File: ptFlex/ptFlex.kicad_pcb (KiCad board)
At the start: 4 copper layers, 30 x 73.5 mm, 70 parts, among them J1 6 Pin Male Header, J2 8 Pin Male Header, Q1 BSS138, Q2 BSS138, Q3 BSS138, Q4 MMBT3904, Q5 DMP2004K-7, U1 LP3985IM5-3.3/NOPB, U2 ATMega 328p-AU, U3 SA818S-V, U4 ATGM336H-5N31, Y1 8MHz

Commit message: Schematic mostly revised for v2.0
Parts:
- removed ANT2a1, ANT2b1: VHF Test Point, Custom DS:Small Test Point Pin
- removed D2: CDBA340L-G Schottky, Diode_SMD:D_SMA
- removed D3: 5.1V Zenor, Diode_SMD:D_SOD-123
- removed J2: 8 Pin Male Header, Connector_PinHeader_2.54mm:PinHeader_2x04_P2.54mm_Vertical
- removed JPV2, PV1: 5.5V 180mW Solar, Custom DS:PowerFilm MPT3.6-75
- removed R14, R15: 10k, Resistor_SMD:R_0805_2012Metric
- added C21: 2.2uF, Capacitor_SMD:C_0805_2012Metric, F.Cu at (215.6, 70.7)
- added C22: 10nF, Capacitor_SMD:C_0805_2012Metric, F.Cu at (215.6, 73.7)
- added C23: 10nF, Capacitor_SMD:C_0805_2012Metric, F.Cu at (215.6, 76.7)
- added C24: 10nF, Capacitor_SMD:C_0805_2012Metric, F.Cu at (215.6, 79.8)
- added J4: Qwiic, Connector_JST:JST_SH_SM04B-SRSS-TB_1x04-1MP_P1.00mm_Horizontal, F.Cu at (108.9, 133.5)
- added J5: 3 Pin Male Header, Connector_PinHeader_2.54mm:PinHeader_1x03_P2.54mm_Vertical, F.Cu at (82.0, 106.4)
- added J6: Barrel_Jack_Switch, Connector_BarrelJack:BarrelJack_CLIFF_FC681465S_SMT_Horizontal, F.Cu at (106.7, 69.4)
- added PZ1: Piezo Buzzer, Buzzer_Beeper:Buzzer_TDK_PS1240P02BT_D12.2mm_H6.5mm, F.Cu at (103.2, 149.5)
- added SW1: Reset Switch, Button_Switch_SMD:SW_SPST_PTS647_Sx38, F.Cu at (93.8, 142.5)
- added U5: LM1086-5.0, Package_TO_SOT_SMD:TO-263-3_TabPin2, F.Cu at (106.8, 87.5)
- added U6: BME280, Package_LGA:Bosch_LGA-8_2.5x2.5mm_P0.65mm_ClockwisePinNumbering, F.Cu at (215.6, 83.5)
- C1: value 6V 1F -> 10nF; footprint Custom DS:CDS CSP Super Cap 8mm dia -> Capacitor_SMD:C_0805_2012Metric; moved to F.Cu
- D1: value CDBA340L-G Schottky -> 1N4007FL; footprint Diode_SMD:D_SMA -> Diode_SMD:D_SOD-123
- Q3: value BSS138 -> MMBT3904
- R1: value 47 -> 1k; footprint Resistor_SMD:R_2512_6332Metric -> Resistor_SMD:R_0805_2012Metric
- U3: moved to F.Cu
- Y1: value 8MHz -> 16MHz
- moved U3 88.9 mm to (65.7, 94.9), turned to 180 degrees
- moved ANT2 88.9 mm to (56.6, 63.5)
- moved U4 85.8 mm to (61.6, 142.1)
- moved Q3 85.6 mm to (227.2, 63.9)
- moved ANT1 84.5 mm to (64.2, 155.3)
- moved D1 83.3 mm to (221.8, 63.1), turned to 0 degrees
- moved C19 82.8 mm to (65.1, 66.3), turned to -90 degrees
- moved C18 80.2 mm to (68.1, 66.3), turned to -90 degrees
- moved C20 80.1 mm to (60.9, 131.9)
- moved Q5 80.1 mm to (65.2, 131.9)
- moved R23 80.1 mm to (69.4, 131.9)
- moved L3 78.1 mm to (66.1, 69.8), turned to -135 degrees
- moved R10 77.8 mm to (75.1, 145.2)
- moved R11 77.8 mm to (75.1, 143.2)
- moved Q1 77.8 mm to (80.1, 144.2)
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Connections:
- C1 pad 1: Net-(D1-K) -> Net-(D4-K)
- C12 pad 1: +3.3V -> Net-(Q5-D)
- C2 pad 1: /BATT-SENSE -> Net-(C2-Pad1)
- C3 pad 1: +BATT -> +5V
- C4 pad 1: +BATT -> +5V
- C5 pad 1: +BATT -> +5V
- C6 pad 1: +BATT -> +5V
- D1 pad 1: Net-(D1-K) -> +5V
- D4 pad 1: +BATT -> Net-(D4-K)
- D4 pad 2: Net-(D1-K) -> Net-(D4-A)
- J1 pad 2: +BATT -> +5V
- Q3 pad 1: +3.3V -> Net-(Q3-B)
- Q3 pad 2: Net-(Q3-S) -> GND
- Q3 pad 3: Net-(Q3-D) -> Net-(D1-A)
- R1 pad 1: Net-(D1-K) -> Net-(Q3-B)
- R1 pad 2: +BATT -> /PIEZO
- R11 pad 2: +BATT -> +5V
- R13 pad 2: +BATT -> +5V
- R18 pad 2: +BATT -> +5V
- R2 pad 1: /BATT-SENSE -> Net-(C2-Pad1)
- R2 pad 2: +BATT -> Net-(D4-K)
- R22 pad 2: Net-(Q1-D) -> Net-(U2-PD4)
- R3 pad 2: /BATT-SENSE -> Net-(C2-Pad1)
- R7 pad 1: +3.3V -> +5V
- R8 pad 2: /SCL -> Net-(J4-Pin_4)
- R9 pad 2: /SDA -> Net-(J4-Pin_3)
- U1 pad 1: +BATT -> +5V
- U1 pad 3: +BATT -> +5V
- U2 pad 13: Net-(Q2-S) -> Net-(U2-PB1)
- U2 pad 14: Net-(Q3-S) -> Net-(U2-PB2)
- U2 pad 18: +3.3V -> +5V
- U2 pad 2: Net-(Q1-S) -> Net-(U2-PD4)
- U2 pad 4: +3.3V -> +5V
- U2 pad 6: +3.3V -> +5V
- U2 pad 9: Net-(J2-Pin_8) -> unconnected-(U2-PD5-Pad9)
- U3 pad 16: Net-(Q2-D) -> Net-(U2-PB1)
- U3 pad 17: Net-(Q3-D) -> Net-(U2-PB2)
- U3 pad 6: Net-(Q1-D) -> Net-(U2-PD4)
- U3 pad 8: +BATT -> +5V
- U4 pad 2: /GPS-RX -> Net-(Q2-S)
- U4 pad 3: /GPS-TX -> Net-(Q1-S)
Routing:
- net +BATT: track 159.3 -> 0.00 mm, vias 9 -> 0
- net Net-(D1-K): track 40.2 -> 0.00 mm, vias 2 -> 0
- net unconnected-(U2-PD5-Pad9): track 0.00 -> 37.5 mm, vias 0 -> 1
- net Net-(J2-Pin_8): track 37.5 -> 0.00 mm, vias 1 -> 0
- net Net-(Q3-D): track 36.2 -> 0.00 mm, vias 1 -> 0
- net /RESET: track 46.2 -> 12.8 mm, vias 3 -> 2
- net Net-(Q3-S): track 28.9 -> 0.00 mm, vias 2 -> 0
- net +3.3V: track 68.0 -> 41.1 mm, vias 9 -> 6
- net /SCK: track 26.9 -> 0.07 mm
- net /SCL: track 29.3 -> 3.88 mm
- net Net-(Q1-D): track 30.2 -> 7.86 mm, vias 2 -> 1
- net /MOSI: track 25.4 -> 3.17 mm, vias 1 -> 0
- net Net-(U3-MIC-IN): track 22.2 -> 0.00 mm, vias 1 -> 0
- net /DIG-PTT: track 29.1 -> 7.57 mm
- net Net-(Q2-D): track 26.6 -> 6.15 mm, vias 1 -> 0
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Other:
- board outline removed

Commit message: PCB nearing final
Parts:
- removed SW1: Reset Switch, Button_Switch_SMD:SW_SPST_PTS647_Sx38
- ANT2: value SMA Edge Mount (Optional) -> SMA Connector; footprint Connector_Coaxial:SMA_Samtec_SMA-J-P-H-ST-EM1_EdgeMount -> Connector_Coaxial:SMB_Jack_Vertical
- C21: value 2.2uF -> 47uF
- moved Q3 158.2 mm to (89.7, 142.2)
- moved D1 157.8 mm to (87.5, 145.9)
- moved C22 155.4 mm to (60.2, 78.3)
- moved R1 154.6 mm to (86.2, 142.2), turned to 90 degrees
- moved C24 133.3 mm to (97.2, 141.1), turned to 180 degrees
- moved U6 133.2 mm to (105.3, 158.3)
- moved C21 130.1 mm to (87.5, 94.0), turned to 180 degrees
- moved C1 130.0 mm to (87.5, 90.3), turned to 180 degrees
- moved C23 129.6 mm to (97.1, 129.4)
- moved C12 107.1 mm to (56.5, 132.6), turned to 90 degrees
- moved R18 101.5 mm to (63.9, 120.1), turned to 0 degrees
- moved C11 99.5 mm to (61.6, 132.6), turned to 90 degrees
- moved D5 99.2 mm to (64.0, 127.8)
- moved R17 99.1 mm to (63.9, 122.8)
- moved D6 98.6 mm to (64.0, 125.4)
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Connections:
- net /GPS-EN renamed GPS-EN
- net /MISO renamed MISO
- net /MOSI renamed MOSI
- net /RESET renamed RESET
- net /SCK renamed SCK
- net /SCL renamed SCL
- net /SDA renamed SDA
- net Net-(U2-PB1) renamed XMIT-TX
- net Net-(U2-PB2) renamed XMIT-RX
- net Net-(U2-PD3) renamed XMIT-TX-AUDIO
- net Net-(U2-PD4) renamed XMIT-POWERSAVE
- C2 pad 1: Net-(C2-Pad1) -> BATT-SENSE
- Q1 pad 3: Net-(Q1-D) -> GPS-TX
- Q2 pad 3: Net-(Q2-D) -> GPS-RX
- R1 pad 2: /PIEZO -> PIEZO
- R11 pad 1: Net-(Q1-D) -> GPS-TX
- R13 pad 1: Net-(Q2-D) -> GPS-RX
- R17 pad 1: /DIG-PTT -> DIG-PTT
- R2 pad 1: Net-(C2-Pad1) -> BATT-SENSE
- R20 pad 2: /DIG-PTT -> XMIT-PTT
- R3 pad 2: Net-(C2-Pad1) -> BATT-SENSE
- R4 pad 1: /DIG-PTT -> XMIT-PTT
- U2 pad 11: /GPS-TX -> GPS-TX
- U2 pad 12: /GPS-RX -> GPS-RX
- U2 pad 24: /BATT-SENSE -> BATT-SENSE
- U2 pad 32: /DIG-PTT -> XMIT-PTT
- U2 pad 9: unconnected-(U2-PD5-Pad9) -> PIEZO
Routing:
- net +3.3V: track 41.1 -> 105.5 mm, vias 6 -> 5
- net XMIT-POWERSAVE: track 12.0 -> 61.5 mm, vias 0 -> 2
- net +5V: track 5.92 -> 52.2 mm, vias 2 -> 11
- net Net-(D4-K): track 0.00 -> 45.2 mm, vias 0 -> 2
- net Net-(Q4-C): track 0.00 -> 42.6 mm
- net SCK: track 0.07 -> 42.6 mm, vias 0 -> 2
- net Net-(U3-HIGH/LOW): track 0.00 -> 39.4 mm
- net unconnected-(U2-PD5-Pad9): track 37.5 -> 0.00 mm, vias 1 -> 0
- net XMIT-PTT: track 0.00 -> 33.3 mm
- net XMIT-TX: track 8.35 -> 36.4 mm, vias 1 -> 2
- net MOSI: track 3.17 -> 28.9 mm, vias 0 -> 1
- net GPS-TX: track 0.00 -> 23.7 mm, vias 0 -> 2
- net BATT-SENSE: track 0.00 -> 23.5 mm
- net XMIT-RX: track 13.2 -> 36.0 mm, vias 1 -> 2
- net Net-(J4-Pin_4): track 0.00 -> 22.1 mm
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- added copper zone on In2.Cu, net +5V
- added copper zone on In1.Cu, net GND
- removed copper zone on In1.Cu, net +3.3V
- removed copper zone on In2.Cu, net GND
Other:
- board outline added: 55 x 100 mm
- board text added: "6-12VDC"
- board text added: "High/Low"
- board text added: "Qwiic"
- board text added: "Status"
- board text added: "Xmit"
- board text added: "ptFlex Tracker - v2.0.0 Custom Digital Services, LLC www.custom-ds.com"
- board text removed: "ptFlex Tracker v1.1.2 Custom Digital Services, LLC www.custom-ds.com"

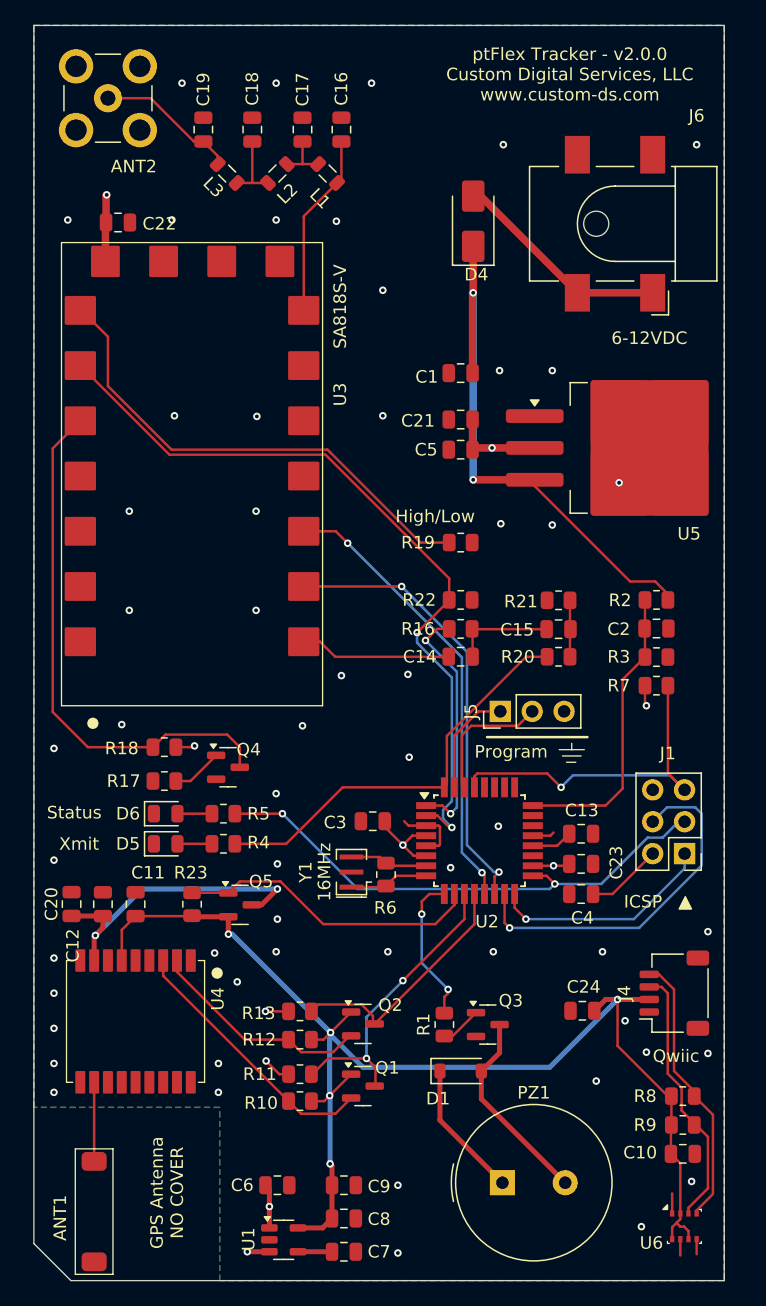
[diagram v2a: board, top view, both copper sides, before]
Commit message: Back filed old versions of PCB from the ptFlex-hardware project into this repo. Shrunk the PCB down by 5mm.
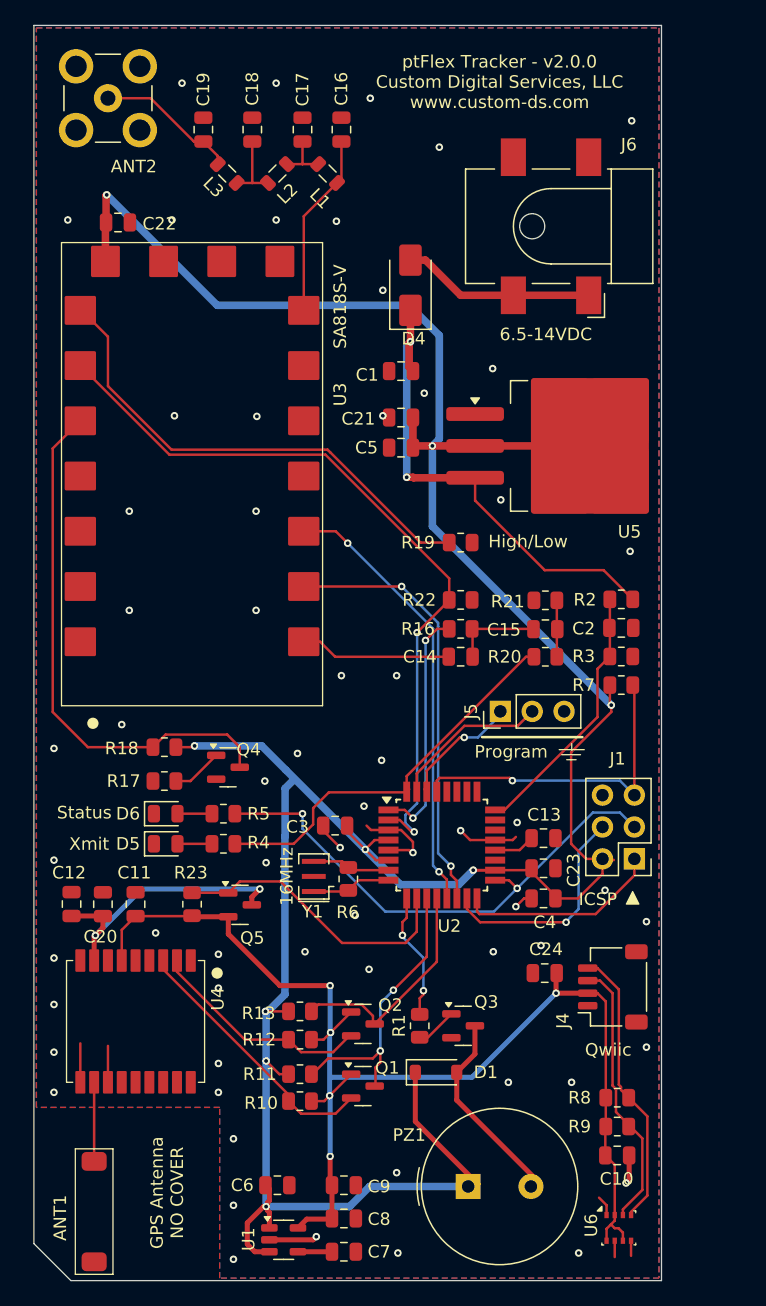
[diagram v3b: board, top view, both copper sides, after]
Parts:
- J5: value 3 Pin Male Header -> Programming
- moved D4 7.14 mm to (83.5, 83.3)
- moved C10 5.23 mm to (100.0, 152.6)
- moved R8 5.23 mm to (100.0, 148.0)
- moved R9 5.23 mm to (100.0, 150.3)
- moved U6 5.23 mm to (100.1, 158.4)
- moved J6 5.10 mm to (94.7, 78.6)
- moved J4 4.93 mm to (99.6, 139.2)
- moved C5 4.75 mm to (82.8, 96.2)
- moved U5 4.75 mm to (96.3, 96.1)
- moved C1 4.75 mm to (82.8, 90.1)
- moved C21 4.75 mm to (82.8, 93.8)
- moved C24 4.24 mm to (94.2, 138.1)
- moved J1 4.02 mm to (101.3, 129.0)
- moved U2 3.02 mm to (86.0, 127.9)
- moved C13 3.02 mm to (94.1, 127.3)
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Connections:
- U2 pad 30: Net-(J5-Pin_2) -> Net-(J5-Pin_1)
- U2 pad 31: Net-(J5-Pin_1) -> Net-(J5-Pin_2)
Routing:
- net +5V: track 52.2 -> 232.8 mm, vias 11 -> 9
- net GND: track 11.4 -> 32.0 mm, vias 55 -> 63
- net MOSI: track 28.9 -> 18.0 mm
- net Net-(D4-K): track 45.2 -> 39.0 mm
- net +3.3V: track 105.5 -> 101.4 mm
- net BATT-SENSE: track 23.5 -> 21.0 mm
- net Net-(Q5-D): track 24.9 -> 22.5 mm
- net Net-(D4-A): track 17.5 -> 15.4 mm
- net Net-(J5-Pin_2): track 10.6 -> 12.7 mm
- net PIEZO: track 11.9 -> 10.2 mm
- net MISO: track 17.9 -> 16.3 mm, vias 1 -> 0
- net GPS-RX: track 19.8 -> 18.2 mm
- net XMIT-PTT: track 33.3 -> 31.8 mm
- net XMIT-RX: track 36.0 -> 34.5 mm
- net Net-(J5-Pin_1): track 8.58 -> 9.95 mm, vias 0 -> 1
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- removed copper zone on In2.Cu, net +5V
- removed copper zone on In1.Cu, net GND
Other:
- board size 55 x 100 mm -> 50 x 100 mm
- copper layers 4 -> 2
- board text added: "6.5-14VDC"
- board text removed: "6-12VDC"

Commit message: Swapped out Piezo symbol. Minor tweaks
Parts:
- added C25: 10nF, Capacitor_SMD:C_0805_2012Metric, F.Cu at (137.1, 121.8)
- PZ1: value Piezo Buzzer -> CEM-1206S; footprint Buzzer_Beeper:Buzzer_TDK_PS1240P02BT_D12.2mm_H6.5mm -> Piezo - CEM-1206S:CUI_CEM-1206S
- R2: value 100k -> 150k
- R3: value 22k -> 10k
- moved PZ1 66.9 mm to (152.8, 138.3)
- moved ANT1 64.6 mm to (120.6, 140.8)
- moved ANT2 64.6 mm to (121.7, 51.6)
- moved C1 64.6 mm to (145.1, 73.4)
- moved C10 64.6 mm to (162.3, 135.9)
- moved C11 64.6 mm to (123.9, 115.9)
- moved C12 64.6 mm to (118.8, 115.8)
- moved C13 64.6 mm to (156.4, 110.6)
- moved C14 64.6 mm to (149.8, 96.1)
- moved C15 64.6 mm to (156.6, 93.9)
- moved C16 64.6 mm to (140.3, 54.1)
- moved C17 64.6 mm to (137.2, 54.1)
- moved C18 64.6 mm to (133.2, 54.1)
- moved C19 64.6 mm to (129.3, 54.1)
- moved C20 64.6 mm to (121.3, 115.9)
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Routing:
- net +5V: track 232.8 -> 229.9 mm
- net +3.3V: track 101.4 -> 103.2 mm
- net GND: track 32.0 -> 30.5 mm, vias 63 -> 67
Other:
- outline, holes or cut-outs redrawn

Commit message: Renumbered all parts.
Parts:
- renumbered C7 to C10, C8 to C11, C9 to C12, C10 to C13, C11 to C14, C25 to C15, C24 to C16, C15 to C17, C14 to C18, C12 to C19, C16 to C21, C17 to C22, C18 to C23, C19 to C24, C13 to C25, C21 to C3, C22 to C4, C23 to C5, C3 to C6, C4 to C7, C5 to C8, C6 to C9, D4 to D1, D5 to D2, D6 to D3, D1 to D4, J6 to J1, J5 to J2, J4 to J3, J1 to J4, Q3 to Q1, Q4 to Q2, Q5 to Q3, Q1 to Q4, Q2 to Q5, R2 to R1, R22 to R10, R20 to R11, R21 to R12, R16 to R13, R17 to R14, R18 to R15, R19 to R16, R23 to R17, R10 to R18, R11 to R19, R3 to R2, R12 to R20, R13 to R21, R4 to R3, R5 to R4, R1 to R5, R8 to R6, R9 to R7, R6 to R8, R7 to R9, U5 to U1, U1 to U2, U2 to U3, U3 to U5

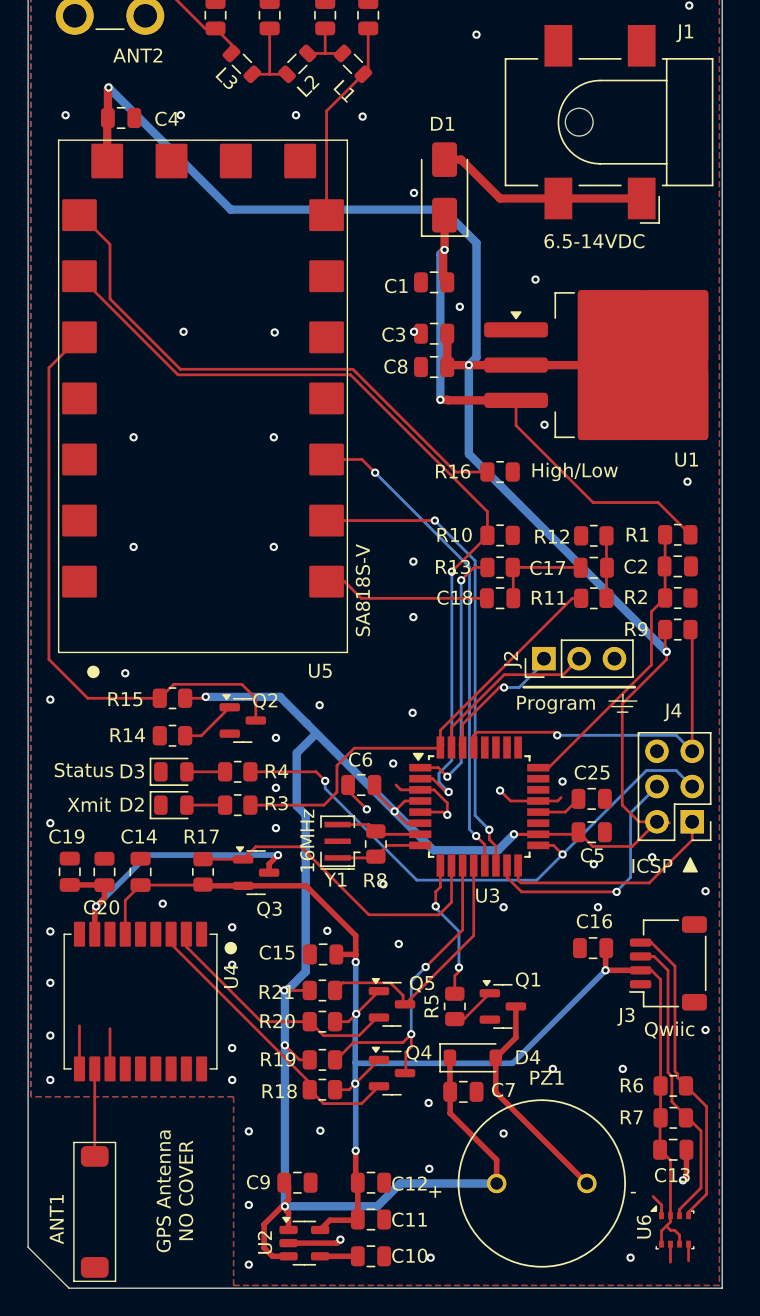
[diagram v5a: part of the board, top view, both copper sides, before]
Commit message: Finalized version 2.0.0 of the PCB to bring it in sync with the ptSolar design.
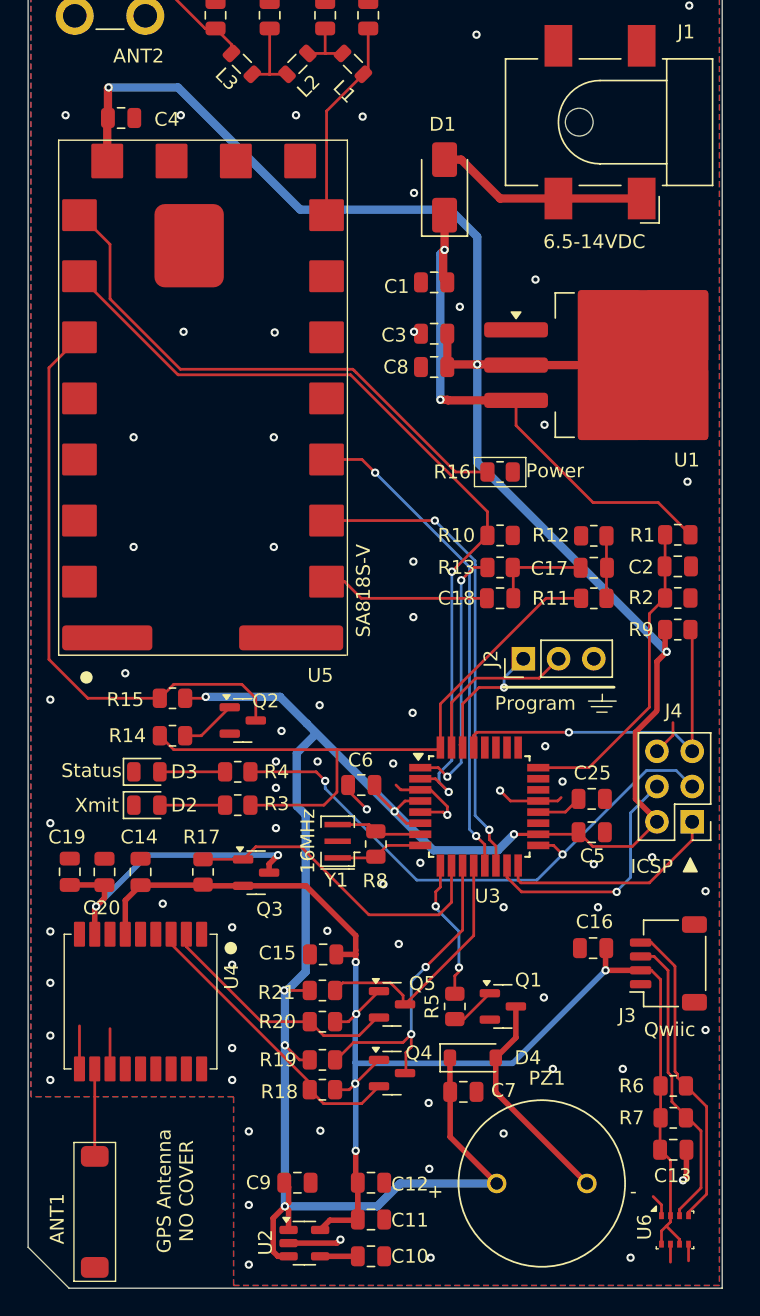
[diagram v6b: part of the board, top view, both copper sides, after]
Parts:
- moved D2 1.95 mm to (124.4, 111.0)
- moved D3 1.95 mm to (124.4, 108.6)
- moved J2 1.49 mm to (151.5, 100.5)
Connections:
- R14 pad 1: DIG-PTT -> XMIT-PTT
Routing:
- net XMIT-PTT: track 32.1 -> 46.8 mm
- net +5V: track 229.9 -> 227.3 mm
- net GND: track 30.5 -> 32.9 mm, vias 67 -> 72
- net Net-(D3-A): track 2.75 -> 4.70 mm
- net Net-(D2-A): track 2.75 -> 4.70 mm
- net BATT-SENSE: track 21.0 -> 22.7 mm
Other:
- board text added: "Power"
- board text removed: "High/Low"
